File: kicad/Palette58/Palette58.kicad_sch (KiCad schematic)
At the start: 64 parts, among them SW1 SW_DPDT_x2, SW2 SW_Push, SW3 SW_DPDT_x2

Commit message: change smd diode footprint to 323
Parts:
- removed D1: D, symbol Device:D
- removed SW3: SW_DPDT_x2, symbol Switch:SW_DPDT_x2
- D30: value D -> 1N5819
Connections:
- net B+: no longer D30.1 (K), SW1.3 (C)
- new net JST+: D30.1 (K), SW1.3 (C)
- no-connect marks 3 -> 2
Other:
- note removed: "3.7V Lipo battery"
- note removed: "Development Board"
- note removed: "Planned Setup"
- note removed: "Standard Setup"

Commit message: Reflect board
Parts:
- added C29, C30, C31, C32, C33, C34, C35, C36, C37, C38, C39, C40, C41, C42, C43, C44, C45, C46, C47, C48, C49, C50, C51, C52, C53, C54, C55, C56: 100nF, symbol Device:C
- added D60: 1N5819, symbol Device:D
- added LED30, LED31, LED32, LED33, LED34, LED35, LED36, LED37, LED38, LED39, LED40, LED41, LED42, LED43, LED44, LED45, LED46, LED47, LED48, LED49, LED50, LED51, LED52, LED53, LED54, LED55, LED56, LED57, LED58: XINGLIGHTXL-1615RGBC-WS2812B, LED_SMD:XINGLIGHT XL-1615RGBC-WS2812B, symbol LED:WS2812B
- added R2: 330Ω, Resistor_SMD:R_0402_1005Metric, symbol Device:R
- added R4: 10kΩ, symbol Device:R
- added SW2: SW_DPDT_x2, symbol Switch:SW_DPDT_x2
- added SW4: SW_Push, symbol Switch:SW_Push
- renumbered D30 to D59, R2 to R3, SW2 to SW3
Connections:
- net B+: now also D60.2 (A), SW2.2 (B)
- net GND: now also C29.2, C30.2, C31.2, C32.2, C33.2, C34.2, C35.2, C36.2, C37.2, C38.2, C39.2, C40.2, C41.2, C42.2, C43.2, C44.2, C45.2, C46.2, C47.2, C48.2, C49.2, C50.2, C51.2, C52.2, C53.2, C54.2, C55.2, C56.2, LED30.3 (VSS), LED31.3 (VSS), LED32.3 (VSS), LED33.3 (VSS), LED34.3 (VSS), LED35.3 (VSS), LED36.3 (VSS), LED37.3 (VSS), LED38.3 (VSS), LED39.3 (VSS), LED40.3 (VSS), LED41.3 (VSS), LED42.3 (VSS), LED43.3 (VSS), LED44.3 (VSS), LED45.3 (VSS), LED46.3 (VSS), LED47.3 (VSS), LED48.3 (VSS), LED49.3 (VSS), LED50.3 (VSS), LED51.3 (VSS), LED52.3 (VSS), LED53.3 (VSS), LED54.3 (VSS), LED55.3 (VSS), LED56.3 (VSS), LED57.3 (VSS), LED58.3 (VSS), SW4.2
- net JST+: now also D60.1 (K), SW2.3 (C)
- net P0.06: now also R2.1
- net RST: now also R4.1, SW4.1
- net VCC: now also C29.1, C30.1, C31.1, C32.1, C33.1, C34.1, C35.1, C36.1, C37.1, C38.1, C39.1, C40.1, C41.1, C42.1, C43.1, C44.1, C45.1, C46.1, C47.1, C48.1, C49.1, C50.1, C51.1, C52.1, C53.1, C54.1, C55.1, C56.1, LED30.1 (VDD), LED31.1 (VDD), LED32.1 (VDD), LED33.1 (VDD), LED34.1 (VDD), LED35.1 (VDD), LED36.1 (VDD), LED37.1 (VDD), LED38.1 (VDD), LED39.1 (VDD), LED40.1 (VDD), LED41.1 (VDD), LED42.1 (VDD), LED43.1 (VDD), LED44.1 (VDD), LED45.1 (VDD), LED46.1 (VDD), LED47.1 (VDD), LED48.1 (VDD), LED49.1 (VDD), LED50.1 (VDD), LED51.1 (VDD), LED52.1 (VDD), LED53.1 (VDD), LED54.1 (VDD), LED55.1 (VDD), LED56.1 (VDD), LED57.1 (VDD), LED58.1 (VDD), R4.2
- new net: LED48.2 (DOUT), LED52.4 (DIN)
- new net: LED44.2 (DOUT), LED48.4 (DIN)
- new net: LED53.4 (DIN), R2.2
- new net: LED40.2 (DOUT), LED44.4 (DIN)
- new net: LED36.2 (DOUT), LED40.4 (DIN)
- new net: LED33.4 (DIN), LED37.2 (DOUT)
- new net: LED37.4 (DIN), LED41.2 (DOUT)
- new net: LED32.4 (DIN), LED33.2 (DOUT)
- new net: LED41.4 (DIN), LED45.2 (DOUT)
- new net: LED30.4 (DIN), LED54.4 (DIN)
- new net: LED51.4 (DIN), LED52.2 (DOUT)
- new net: LED57.2 (DOUT), LED58.4 (DIN)
- new net: LED39.4 (DIN), LED43.2 (DOUT)
- new net: LED43.4 (DIN), LED47.2 (DOUT)
- new net: LED32.2 (DOUT), LED36.4 (DIN)
- new net: LED31.4 (DIN), LED35.2 (DOUT)
- new net: LED35.4 (DIN), LED39.2 (DOUT)
- new net: LED55.2 (DOUT), LED56.4 (DIN)
- new net: LED54.2 (DOUT), LED55.4 (DIN)
- new net: LED47.4 (DIN), LED51.2 (DOUT)
- new net: LED49.4 (DIN), LED53.2 (DOUT)
- new net: LED45.4 (DIN), LED49.2 (DOUT)
- new net: LED56.2 (DOUT), LED57.4 (DIN)
- no-connect marks 2 -> 4
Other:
- moved on the sheet: C1, C10, C11, C12, C13, C14, C15, C16, C17, C18, C19, C2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

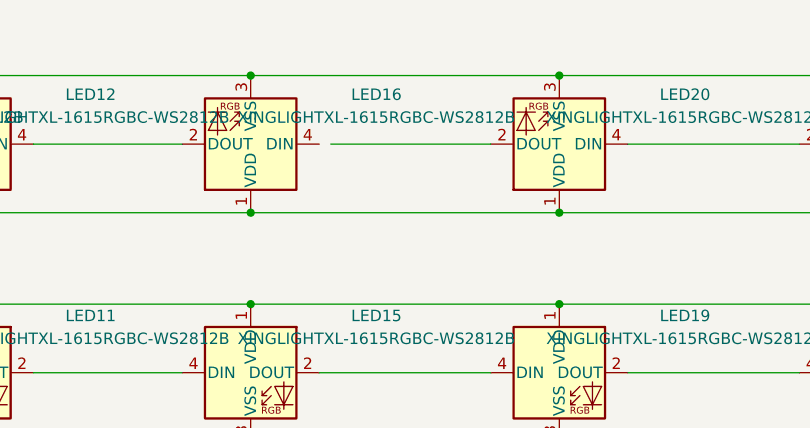
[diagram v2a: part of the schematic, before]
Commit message: Route left half
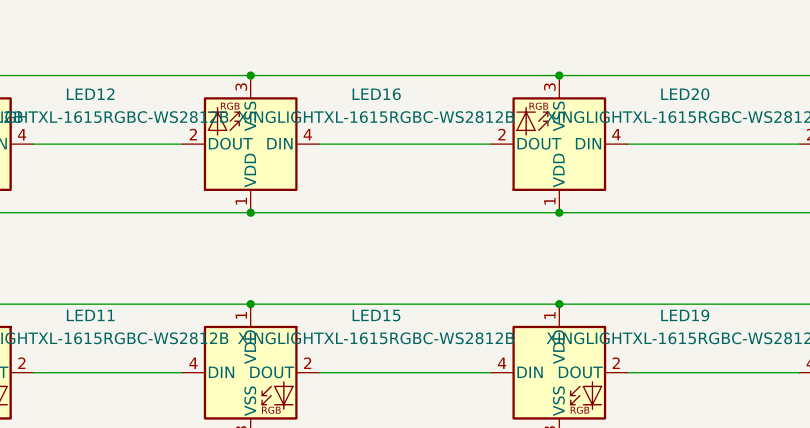
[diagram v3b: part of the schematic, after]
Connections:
- net at LED16.4 (DIN): now also LED20.2 (DOUT)
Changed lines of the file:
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@@
-	(wire
-		(pts
-			(xy 143.51 30.48) (xy 161.29 30.48)
-		)
-		(stroke
-			(width 0)
-			(type default)
-		)
-	)
 	(wire
 		(pts
@@
 		)
 		(stroke
+			(width 0)
+			(type default)
+		)
+	)
+	(wire
+		(pts
+			(xy 142.24 30.48) (xy 161.29 30.48)
+		)
+		(stroke

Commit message: Finish Routing
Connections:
- net at LED38.2 (DOUT): now also LED42.4 (DIN)
- net at LED38.4 (DIN): now also LED34.2 (DOUT)
- net at LED30.2 (DOUT): now also LED34.4 (DIN)
- net at LED30.4 (DIN): now also LED31.2 (DOUT); no longer LED54.4 (DIN)
- net at LED46.2 (DOUT): now also LED50.4 (DIN)
- net at LED46.4 (DIN): now also LED42.2 (DOUT)
- net at LED50.2 (DOUT): now also LED54.4 (DIN)
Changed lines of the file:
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@@
+	(wire
+		(pts
+			(xy 355.6 106.68) (xy 381 106.68)
+		)
+		(stroke
+			(width 0)
+			(type default)
+		)
+	)
 	(wire
 		(pts
@@
 	(wire
 		(pts
-			(xy 556.26 106.68) (xy 561.34 106.68)
-		)
-		(stroke
-			(width 0)
-			(type default)
-		)
-	)
-	(wire
-		(pts
 			(xy 477.52 30.48) (xy 501.65 30.48)
 		)
@@
 	(wire
 		(pts
+			(xy 477.52 106.68) (xy 501.65 106.68)
+		)
+		(stroke
+			(width 0)
+			(type default)
+		)
+	)
+	(wire
+		(pts
 			(xy 355.6 278.13) (xy 368.3 278.13)
 		)
@@
 	(wire
 		(pts
+			(xy 436.88 106.68) (xy 462.28 106.68)
+		)
+		(stroke
+			(width 0)
+			(type default)
+		)
+	)
+	(wire
+		(pts
 			(xy 26.67 22.86) (xy 38.1 22.86)
 		)
@@
 	(wire
 		(pts
+			(xy 340.36 106.68) (xy 314.96 106.68)
+		)
+		(stroke
+			(width 0)
+			(type default)
+		)
+	)
+	(wire
+		(pts
 			(xy 317.5 245.11) (xy 330.2 245.11)
 		)
@@
 	(wire
 		(pts
+			(xy 314.96 124.46) (xy 492.76 124.46)
+		)
+		(stroke
+			(width 0)
+			(type default)
+		)
+	)
+	(wire
+		(pts
 			(xy 561.34 245.11) (xy 575.31 245.11)
 		)
@@
 	(wire
 		(pts
+			(xy 516.89 106.68) (xy 541.02 106.68)
+		)
+		(stroke
+			(width 0)
+			(type default)
+		)
+	)
+	(wire
+		(pts
+			(xy 556.26 81.28) (xy 556.26 106.68)
+		)
+		(stroke
+			(width 0)
+			(type default)
+		)
+	)
+	(wire
+		(pts
 			(xy 355.6 30.48) (xy 382.27 30.48)
 		)
@@
 	(wire
 		(pts
-			(xy 561.34 106.68) (xy 561.34 143.51)
-		)
-		(stroke
-			(width 0)
-			(type default)
-		)
-	)
-	(wire
-		(pts
 			(xy 210.82 121.92) (xy 30.48 121.92)
 		)
@@
 	(wire
 		(pts
-			(xy 561.34 143.51) (xy 492.76 143.51)
-		)
-		(stroke
-			(width 0)
-			(type default)
-		)
-	)
-	(wire
-		(pts
 			(xy 626.11 278.13) (xy 640.08 278.13)
 		)
@@
 	(wire
 		(pts
+			(xy 492.76 124.46) (xy 492.76 143.51)
+		)
+		(stroke
+			(width 0)
+			(type default)
+		)
+	)
+	(wire
+		(pts
 			(xy 393.7 270.51) (xy 406.4 270.51)
 		)
@@
 	(wire
 		(pts
+			(xy 396.24 106.68) (xy 421.64 106.68)
+		)
+		(stroke
+			(width 0)
+			(type default)
+		)
+	)
+	(wire
+		(pts
 			(xy 27.94 223.52) (xy 21.59 223.52)
 		)
@@
 		)
 		(stroke
+			(width 0)
+			(type default)
+		)
+	)
+	(wire
+		(pts
+			(xy 314.96 106.68) (xy 314.96 124.46)
+		)
+		(stroke
